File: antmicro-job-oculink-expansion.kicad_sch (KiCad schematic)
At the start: 104 parts, among them J1 OCuLink_x4_Amphenol_G14A42121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, J2 Plug_Samtec_ERM8_2x40_ERM8-04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, U1 MAX3373EEKA+, U2 PI3EQX16904GL, U3 PI3EQX16904GL

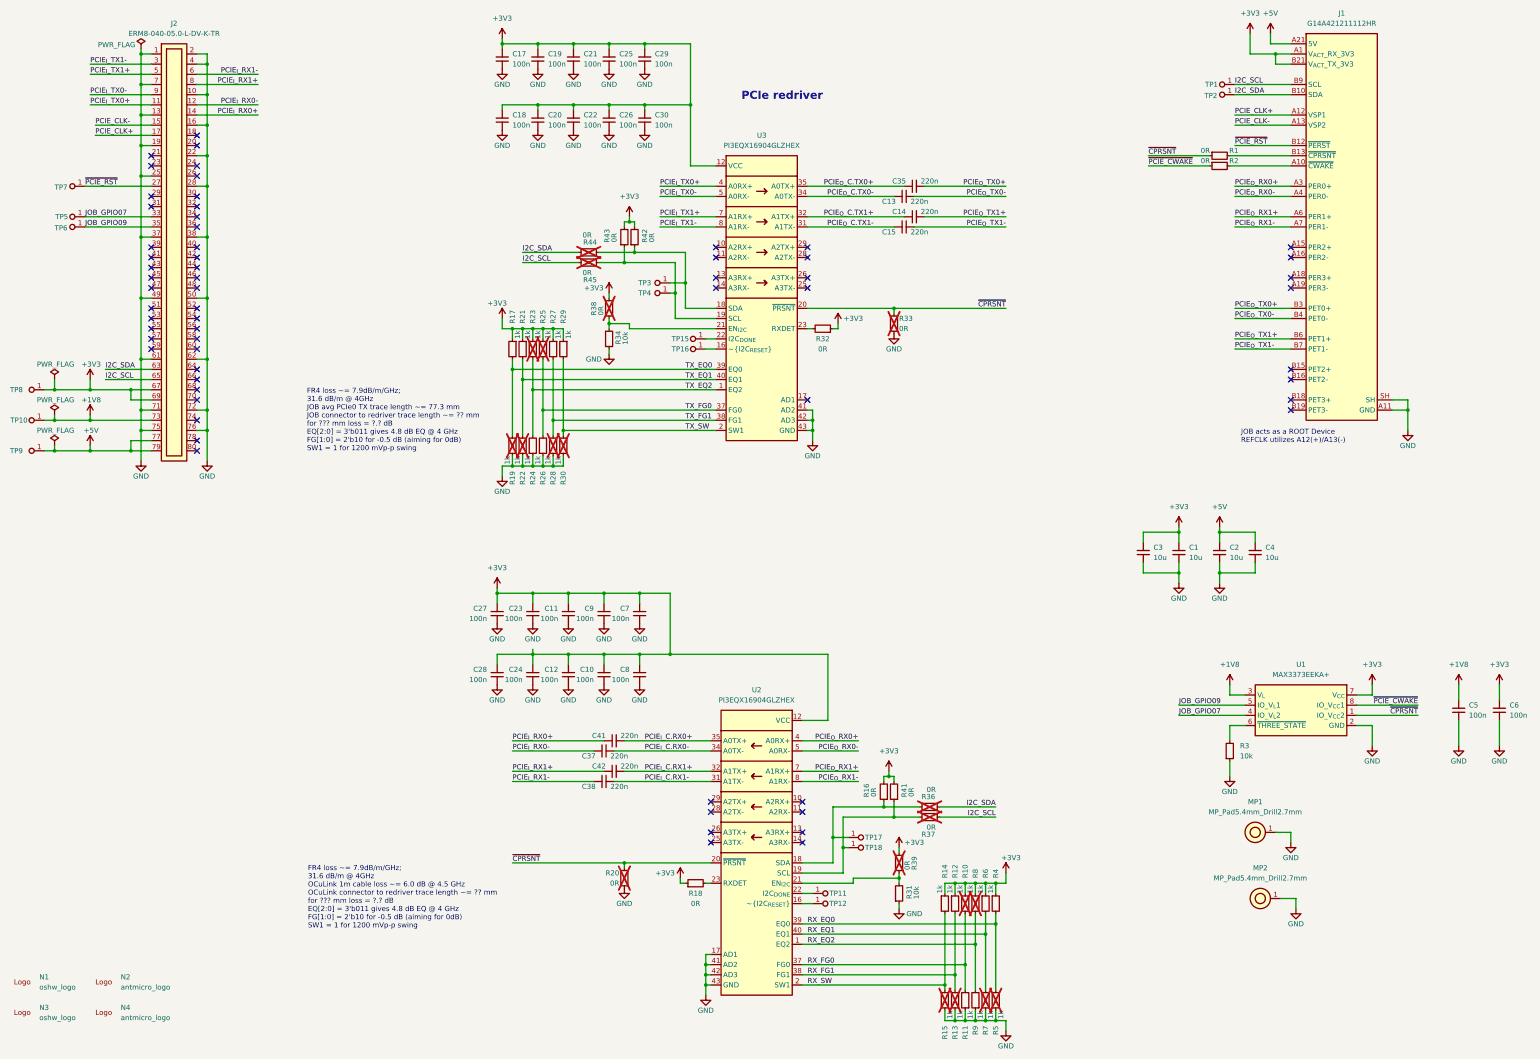
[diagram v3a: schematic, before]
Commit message: [#76297] Connect 1K pull-down to CPRSNT#
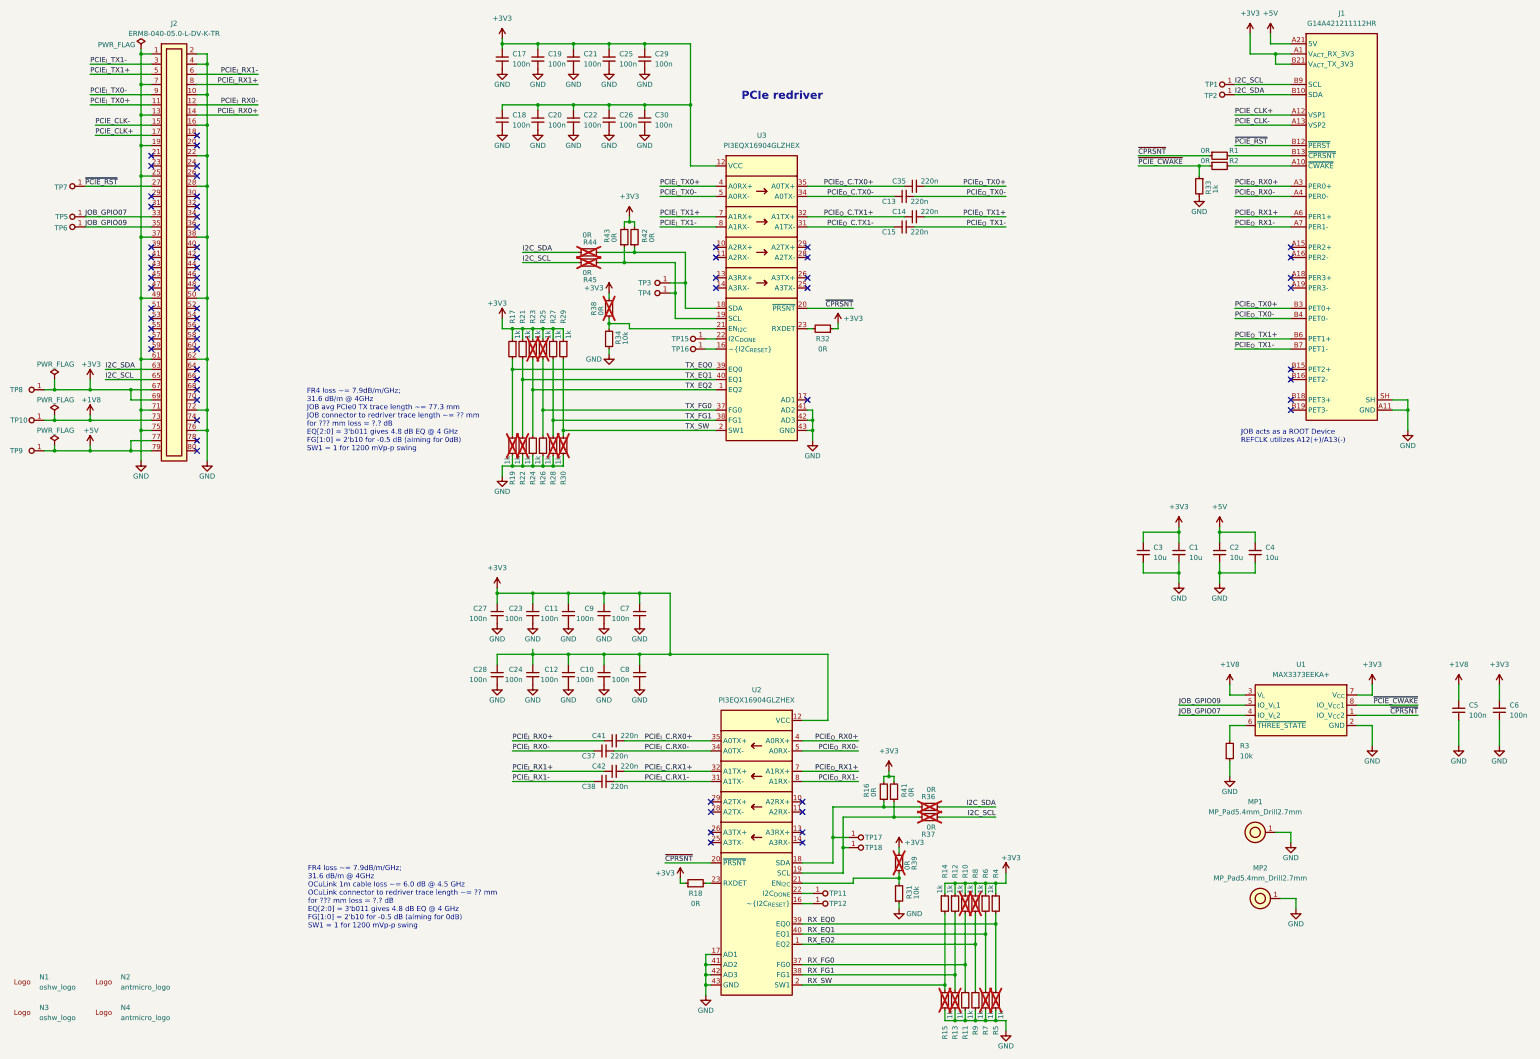
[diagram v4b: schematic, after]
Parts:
- removed R20, R33: R_0R_0402, antmicro-footprints:R_0402_1005Metric, symbol antmicroResistors0402:R_0R_0402
- added R33: R_1k_0402, antmicro-footprints:R_0402_1005Metric, symbol antmicroResistors0402:R_1k_0402
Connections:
- net GND: now also R33.2
- net ~{PCIE_CWAKE}: now also R33.1

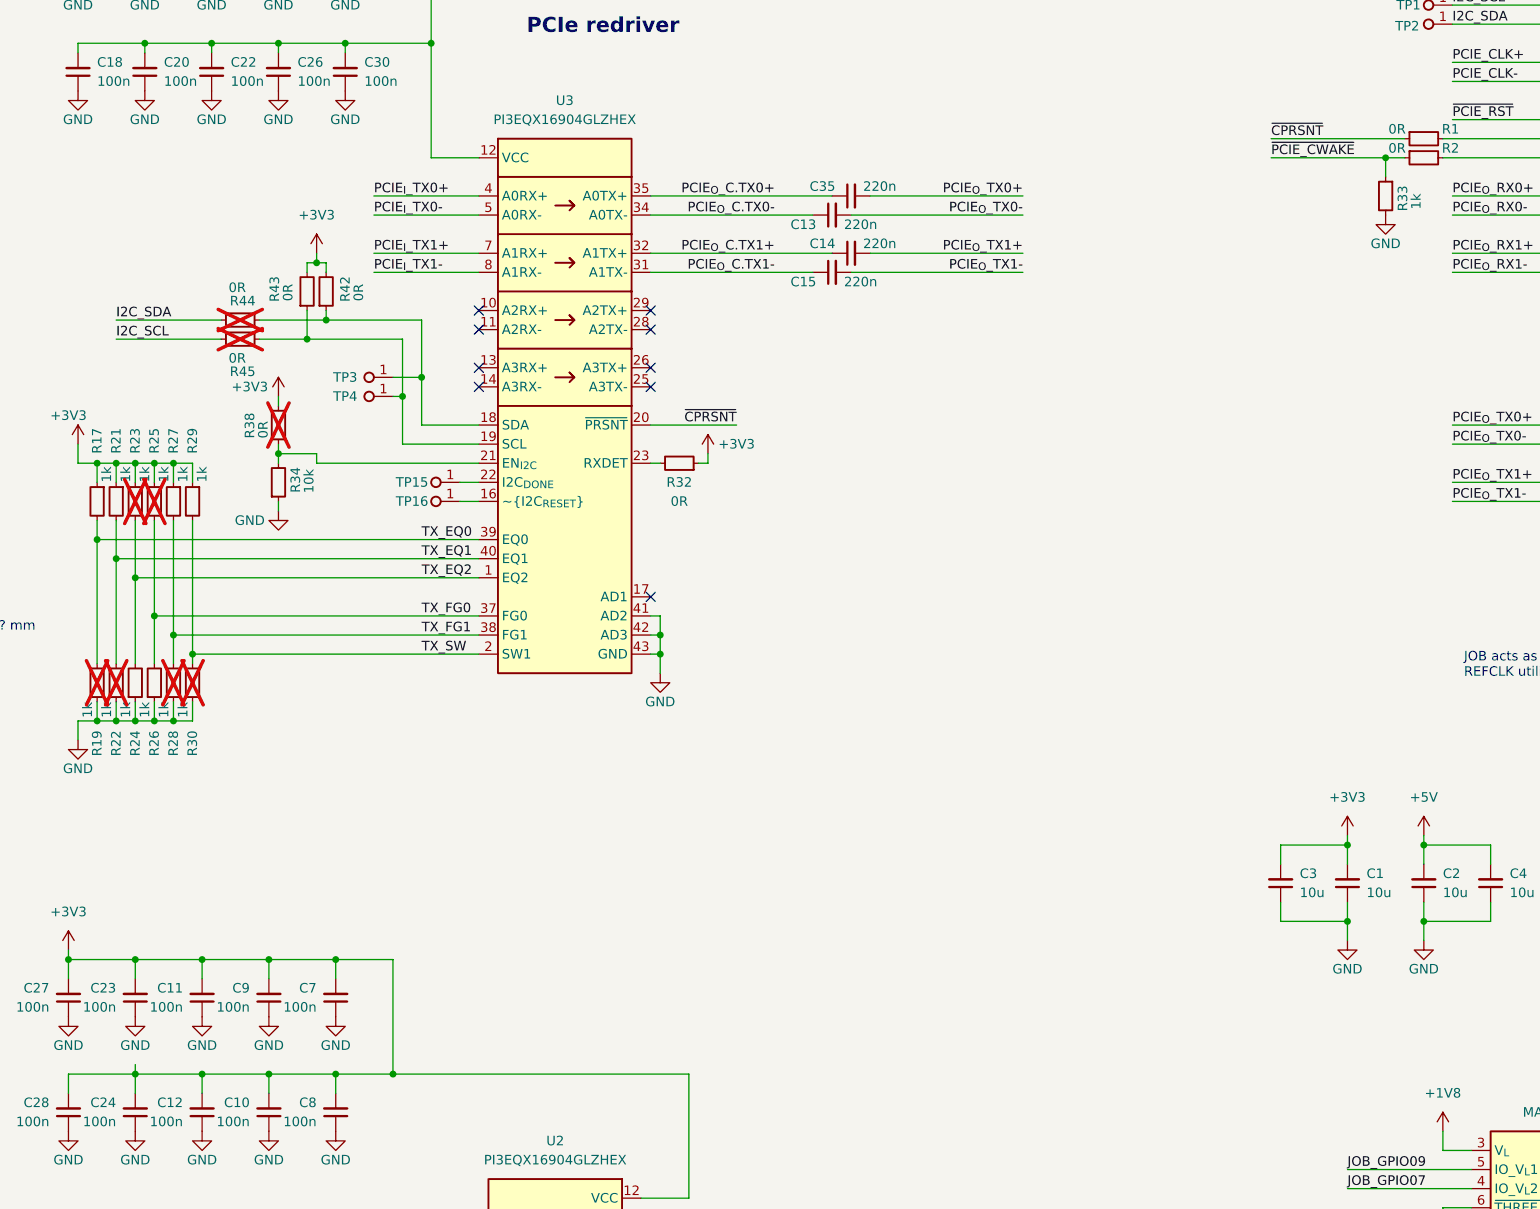
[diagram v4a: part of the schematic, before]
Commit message: [#76297] Clean up unconnected traces
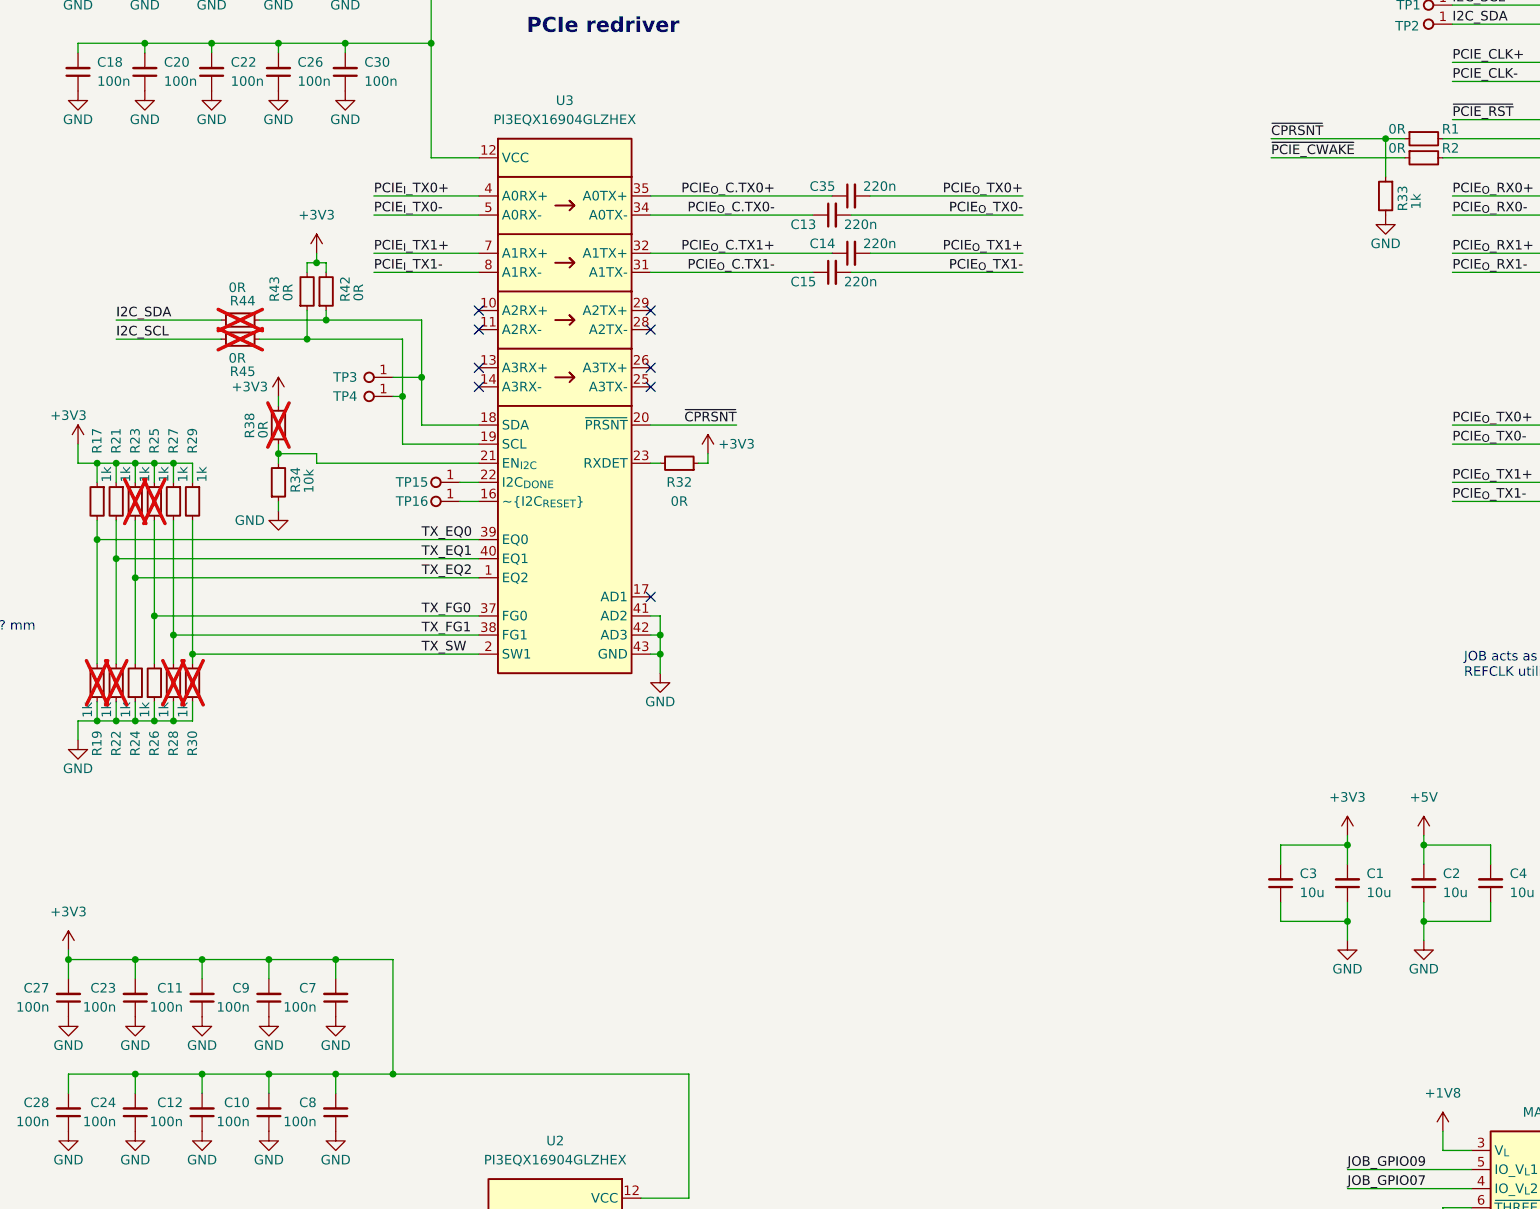
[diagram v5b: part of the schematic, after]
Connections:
- net ~{CPRSNT}: now also R33.1
- net ~{PCIE_CWAKE}: no longer R33.1
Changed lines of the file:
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@@
 	)
 	(junction
+		(at 321.31 55.88)
+		(diameter 0)
+		(color 0 0 0 0)
+	)
+	(junction
 		(at 57.15 106.68)
 		(diameter 0)
@@
 	)
 	(junction
-		(at 321.31 58.42)
-		(diameter 0)
-		(color 0 0 0 0)
-	)
-	(junction
 		(at 245.11 220.98)
 		(diameter 0)
@@
 	(wire
 		(pts
+			(xy 321.31 55.88) (xy 323.85 55.88)
+		)
+		(stroke
+			(width 0)
+			(type default)
+		)
+	)
+	(wire
+		(pts
 			(xy 44.45 43.18) (xy 59.69 43.18)
 		)
@@
 	(wire
 		(pts
-			(xy 306.07 55.88) (xy 323.85 55.88)
+			(xy 306.07 55.88) (xy 321.31 55.88)
 		)
 		(stroke
@@
 	(wire
 		(pts
-			(xy 306.07 58.42) (xy 321.31 58.42)
-		)
-		(stroke
-			(width 0)
-			(type default)
-		)
-	)
-	(wire
-		(pts
 			(xy 149.86 99.06) (xy 147.32 99.06)
 		)
@@
 	(wire
 		(pts
+			(xy 306.07 58.42) (xy 323.85 58.42)
+		)
+		(stroke
+			(width 0)
+			(type default)
+		)
+	)
+	(wire
+		(pts
 			(xy 162.56 124.46) (xy 200.66 124.46)
 		)
@@
 	(wire
 		(pts
-			(xy 321.31 58.42) (xy 323.85 58.42)
-		)
-		(stroke
-			(width 0)
-			(type default)
-		)
-	)
-	(wire
-		(pts
 			(xy 340.36 30.48) (xy 344.17 30.48)
 		)
@@
 	(wire
 		(pts
-			(xy 154.94 180.34) (xy 154.94 179.07)
+			(xy 71.12 38.1) (xy 86.36 38.1)
 		)
 		(stroke
@@
 	(wire
 		(pts
-			(xy 71.12 38.1) (xy 86.36 38.1)
+			(xy 321.31 55.88) (xy 321.31 60.96)
 		)
 		(stroke
@@
 		)
 		(stroke
-			(width 0)
-			(type default)
-		)
-	)
-	(wire
-		(pts
-			(xy 321.31 58.42) (xy 321.31 60.96)
-		)
-		(stroke

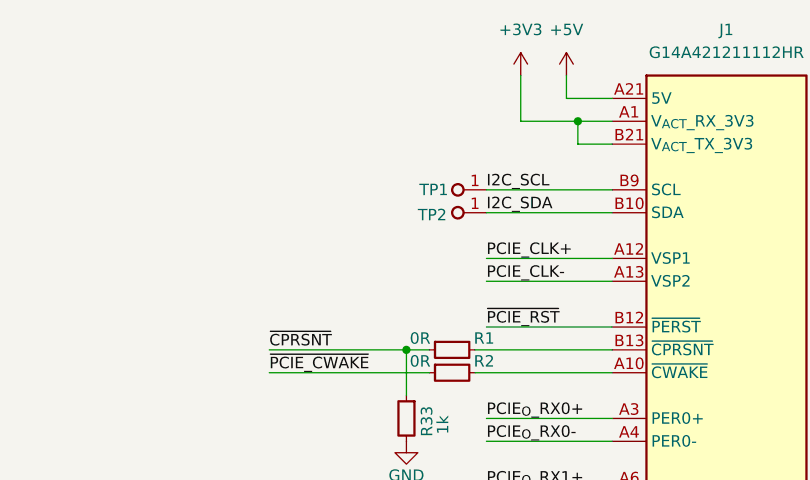
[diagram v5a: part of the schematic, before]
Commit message: [#76297] Add 0R to OCuLink SDA and SCL
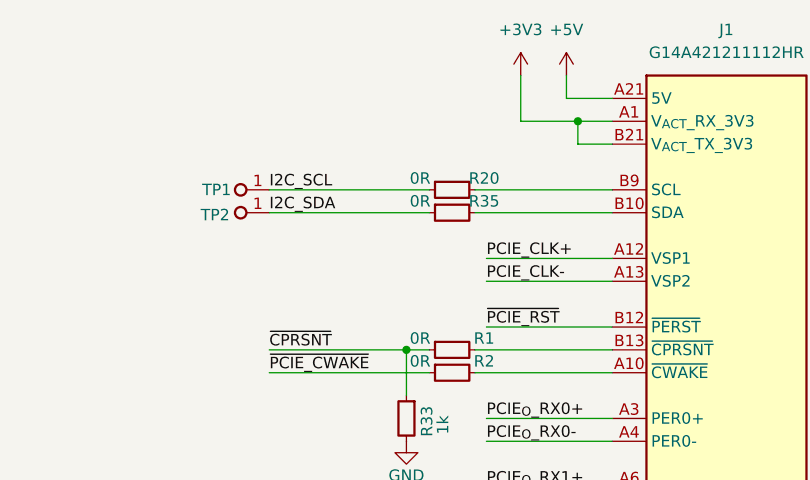
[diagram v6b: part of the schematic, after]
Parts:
- added R20, R35: R_0R_0402, antmicro-footprints:R_0402_1005Metric, symbol antmicroResistors0402:R_0R_0402
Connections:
- net I2C_SCL: now also R20.1; no longer J1.B9 (SCL)
- net I2C_SDA: now also R35.1; no longer J1.B10 (SDA)
- new net: J1.B9 (SCL), R20.2
- new net: J1.B10 (SDA), R35.2
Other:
- moved on the sheet: TP1, TP2
